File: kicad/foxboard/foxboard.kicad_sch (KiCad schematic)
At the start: 188 parts, among them J1 USB_mini_micro_B, K1 KEYSW, K10 KEYSW, K11 KEYSW, K12 KEYSW, K13 KEYSW, K14 KEYSW, K15 KEYSW, K16 KEYSW, K17 KEYSW, K18 KEYSW, K19 KEYSW, K2 KEYSW, K20 KEYSW, K21 KEYSW, K22 KEYSW, K23 KEYSW, K24 KEYSW, K25 KEYSW, K26 KEYSW, K27 KEYSW, K28 KEYSW, K29 KEYSW, K3 KEYSW, K30 KEYSW, K31 KEYSW, K32 KEYSW, K33 KEYSW, K34 KEYSW, K35 KEYSW, K36 KEYSW, K37 KEYSW, K38 KEYSW, K39 KEYSW, K4 KEYSW, K40 KEYSW, K41 KEYSW, K42 KEYSW, K43 KEYSW, K44 KEYSW, K45 KEYSW, K46 KEYSW, K47 KEYSW, K48 KEYSW, K49 KEYSW, K5 KEYSW, K50 KEYSW, K51 KEYSW, K52 KEYSW, K53 KEYSW, K54 KEYSW, K55 KEYSW, K56 KEYSW, K57 KEYSW, K58 KEYSW, K59 KEYSW, K6 KEYSW, K60 KEYSW, K61 KEYSW, K62 KEYSW, K63 KEYSW, K64 KEYSW, K65 KEYSW, K66 KEYSW, K67 KEYSW, K68 KEYSW, K69 KEYSW, K7 KEYSW, K70 KEYSW, K71 KEYSW, K72 KEYSW, K73 KEYSW, K74 KEYSW, K75 KEYSW, K76 KEYSW, K77 KEYSW, K78 KEYSW, K79 KEYSW, K8 KEYSW, K80 KEYSW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

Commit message: update
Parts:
- removed 10k: R1, symbol Device:R
- removed C1, C2: 22p, symbol Device:C_Small
- removed C8: 1U, symbol Device:C
- removed J1: USB_mini_micro_B, symbol keyboard_parts:USB_mini_micro_B
- removed R2: 10k, symbol Device:R
- removed R3, R4: 22, symbol Device:R
- removed SW1: SW_PUSH, symbol keyboard_parts:SW_PUSH
- removed U1: ATMEGA32U4, symbol keyboard_parts:ATMEGA32U4
- removed X1: XTAL_GND, symbol keyboard_parts:XTAL_GND
- added J2: USB_C_Receptacle_USB2.0, Connector_USB:USB_C_Receptacle_Amphenol_12401548E4-2A, symbol Connector:USB_C_Receptacle_USB2.0
- added R5, R6: 5k1, Resistor_SMD:R_0805_2012Metric_Pad1.20x1.40mm_HandSolder, symbol Device:R
- added U2: Teensy4.1, teensy:Teensy41, symbol teensy:Teensy4.1
- C3, C4, C5, C6: footprint (none) -> Capacitor_SMD:C_0201_0603Metric_Pad0.64x0.40mm_HandSolder
- C7: value 4.7i -> 4.7u; footprint (none) -> Capacitor_SMD:C_0201_0603Metric_Pad0.64x0.40mm_HandSolder
- D1, D10, D11, D12, D13, D14, D15, D16, D17, D18, D19, D2, D20, D21, D22, D23, D24, D25, D26, D27, D28, D29, D3, D30, D31, D32, D33, D34, D35, D36, D37, D38, D39, D4, D40, D41, D42, D43, D44, D45, D46, D47, D48, D49, D5, D50, D51, D52, D53, D54, D55, D56, D57, D58, D59, D6, D60, D61, D62, D63, D64, D65, D66, D67, D68, D69, D7, D70, D71, D72, D73, D74, D75, D76, D77, D78, D79, D8, D80, D81, D82, D83, D84, D85, D86, D9: footprint (none) -> Diode_SMD:D_0201_0603Metric_Pad0.64x0.40mm_HandSolder
- K1, K2, K3, K5, K6, K7, K8: footprint (none) -> PCM_marbastlib-mx:SW_MX_1.25u
- K10, K11, K13, K14, K15, K16, K17, K18, K19, K20, K21, K22, K24, K26, K27, K28, K29, K30, K31, K32, K33, K34, K35, K36, K39, K40, K41, K42, K43, K44, K45, K46, K47, K48, K49, K50, K52, K53, K54, K55, K56, K57, K58, K59, K60, K61, K62, K63, K64, K65, K66, K67, K68, K70, K71, K72, K73, K74, K75, K76, K77, K78, K79, K80, K81, K82, K83, K84, K85, K86, K9: footprint (none) -> PCM_marbastlib-mx:SW_MX_1u
- K12, K23: footprint (none) -> PCM_marbastlib-xp-plate-mx:Plate_MX_SPLIT-RSHIFT
- K25: footprint (none) -> PCM_marbastlib-mx:STAB_MX_2.25u
- K37: footprint (none) -> PCM_marbastlib-mx:STAB_MX_ISO
- K38, K51: footprint (none) -> PCM_marbastlib-mx:SW_MX_1.75u
- K4: footprint (none) -> Mounting_Keyboard_Stabilizer:Stabilizer_Cherry_MX_6.25u
- K69: footprint (none) -> PCM_marbastlib-mx:STAB_MX_2.75u
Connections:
- net +5V: now also R5.1, R6.1
- net at K20.1, K33.1, K45.1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: now also K5.1; no longer K8.1
- net at K21.1, K34.1, K46.1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: now also K6.1
- net at K18.1, K31.1, K43.1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: no longer K6.1
- net at K19.1, K32.1, K44.1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: no longer K7.1
- net at K23.1, K36.1, K49.1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: now also K8.1
- net at K22.1: now also K35.1, K48.1, K65.1, K7.1, K80.1
- net at K16.1, K29.1, K41.1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: no longer K5.1
- net at K15.1, K28.1, K40.1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: no longer K4.1
- net at K17.1, K30.1, K42.1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: now also K4.1
- new net: J2.A1 (GND), J2.A12 (GND), J2.B1 (GND), J2.B12 (GND), J2.S1 (SHIELD), U2.47 (GND)
- new net: J2.A4 (VBUS), J2.A9 (VBUS), J2.B4 (VBUS), J2.B9 (VBUS), U2.48 (VIN)
- new net: J2.A7 (D-), J2.B7 (D-), U2.66 (D-)
- new net: J2.A6 (D+), J2.B6 (D+), U2.67 (D+)
- new net: J2.A5 (CC1), R5.2
- new net: J2.B5 (CC2), R6.2
- no-connect marks 0 -> 2
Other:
- moved on the sheet: D4, D5, D6, D7, D8, K4, K5, K6, K7, K8

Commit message: update
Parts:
- added D87: D, symbol Device:D
- added K87: KEYSW, PCM_marbastlib-mx:SW_MX_1u, symbol keyboard_parts:KEYSW
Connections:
- net at D54.1 (K), D55.1 (K), D56.1 (K)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: now also D87.1 (K)
- net at K51.1, K84.1, K9.1: now also K87.1; no longer K68.1
- net at K83.1: now also K68.1
- new net: D87.2 (A), K87.2
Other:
- moved on the sheet: D68, K68
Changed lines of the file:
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@@
   (junction (at 41.91 144.78) (diameter 0) (color 0 0 0 0)
   )
+  (junction (at 298.45 55.88) (diameter 0) (color 0 0 0 0)
+  )
   (junction (at 60.96 71.12) (diameter 0) (color 0 0 0 0)
   )
@@
   (junction (at 214.63 63.5) (diameter 0) (color 0 0 0 0)
   )
+  (junction (at 341.63 24.13) (diameter 0) (color 0 0 0 0)
+  )
   (junction (at 241.3 166.37) (diameter 0) (color 0 0 0 0)
   )
+  (junction (at 342.9 60.96) (diameter 0) (color 0 0 0 0)
+  )
   (junction (at 276.86 55.88) (diameter 0) (color 0 0 0 0)
   )
@@
   (junction (at 135.89 71.12) (diameter 0) (color 0 0 0 0)
   )
+  (junction (at 326.39 55.88) (diameter 0) (color 0 0 0 0)
+  )
   (junction (at 119.38 107.95) (diameter 0) (color 0 0 0 0)
   )
@@
   (junction (at 123.19 36.83) (diameter 0) (color 0 0 0 0)
   )
+  (junction (at 313.69 25.4) (diameter 0) (color 0 0 0 0)
+  )
   (junction (at 363.22 25.4) (diameter 0) (color 0 0 0 0)
   )
@@
   (junction (at 76.2 97.79) (diameter 0) (color 0 0 0 0)
   )
+  (junction (at 341.63 43.18) (diameter 0) (color 0 0 0 0)
+  )
   (junction (at 196.85 63.5) (diameter 0) (color 0 0 0 0)
   )
@@
   (junction (at 347.98 55.88) (diameter 0) (color 0 0 0 0)
   )
-  (junction (at 341.63 24.13) (diameter 0) (color 0 0 0 0)
-  )
   (junction (at 181.61 71.12) (diameter 0) (color 0 0 0 0)
   )
@@
   (junction (at 257.81 55.88) (diameter 0) (color 0 0 0 0)
   )
-  (junction (at 327.66 55.88) (diameter 0) (color 0 0 0 0)
-  )
   (junction (at 113.03 63.5) (diameter 0) (color 0 0 0 0)
   )
@@
   (junction (at 199.39 71.12) (diameter 0) (color 0 0 0 0)
   )
-  (junction (at 342.9 60.96) (diameter 0) (color 0 0 0 0)
-  )
   (junction (at 259.08 78.74) (diameter 0) (color 0 0 0 0)
   )
@@
   (junction (at 62.23 25.4) (diameter 0) (color 0 0 0 0)
   )
-  (junction (at 342.9 44.45) (diameter 0) (color 0 0 0 0)
-  )
   (no_connect (at 242.57 153.67))
   (no_connect (at 242.57 151.13))
@@
     (stroke (width 0) (type default))
   )
+  (wire (pts (xy 326.39 50.8) (xy 326.39 55.88))
+    (stroke (width 0) (type default))
+  )
   (wire (pts (xy 218.44 45.72) (xy 218.44 33.02))
     (stroke (width 0) (type default))
@@
     (stroke (width 0) (type default))
   )
-  (wire (pts (xy 327.66 55.88) (xy 347.98 55.88))
-    (stroke (width 0) (type default))
-  )
   (wire (pts (xy 80.01 106.68) (xy 80.01 107.95))
     (stroke (width 0) (type default))
@@
     (stroke (width 0) (type default))
   )
-  (wire (pts (xy 342.9 44.45) (xy 342.9 60.96))
-    (stroke (width 0) (type default))
-  )
   (wire (pts (xy 222.25 55.88) (xy 240.03 55.88))
     (stroke (width 0) (type default))
@@
     (stroke (width 0) (type default))
   )
-  (wire (pts (xy 327.66 44.45) (xy 327.66 45.72))
+  (wire (pts (xy 297.18 44.45) (xy 298.45 44.45))
     (stroke (width 0) (type default))
   )
@@
     (stroke (width 0) (type default))
   )
+  (wire (pts (xy 341.63 24.13) (xy 341.63 43.18))
+    (stroke (width 0) (type default))
+  )
   (wire (pts (xy 80.01 46.99) (xy 80.01 48.26))
     (stroke (width 0) (type default))
@@
     (stroke (width 0) (type default))
   )
+  (wire (pts (xy 326.39 55.88) (xy 347.98 55.88))
+    (stroke (width 0) (type default))
+  )
   (wire (pts (xy 170.18 36.83) (xy 195.58 36.83))
     (stroke (width 0) (type default))
   )
+  (wire (pts (xy 312.42 43.18) (xy 312.42 44.45))
+    (stroke (width 0) (type default))
+  )
   (wire (pts (xy 157.48 96.52) (xy 157.48 99.06))
     (stroke (width 0) (type default))
@@
     (stroke (width 0) (type default))
   )
+  (wire (pts (xy 341.63 43.18) (xy 342.9 43.18))
+    (stroke (width 0) (type default))
+  )
   (wire (pts (xy 138.43 15.24) (xy 138.43 26.67))
     (stroke (width 0) (type default))
@@
     (stroke (width 0) (type default))
   )
-  (wire (pts (xy 341.63 24.13) (xy 341.63 40.64))
-    (stroke (width 0) (type default))
-  )
   (wire (pts (xy 240.03 176.53) (xy 242.57 176.53))
     (stroke (width 0) (type default))
@@
     (stroke (width 0) (type default))
   )
+  (wire (pts (xy 312.42 43.18) (xy 313.69 43.18))
+    (stroke (width 0) (type default))
+  )
   (wire (pts (xy 347.98 107.95) (xy 347.98 104.14))
     (stroke (width 0) (type default))
@@
     (stroke (width 0) (type default))
   )
-  (wire (pts (xy 341.63 40.64) (xy 342.9 40.64))
-    (stroke (width 0) (type default))
-  )
   (wire (pts (xy 257.81 54.61) (xy 257.81 55.88))
     (stroke (width 0) (type default))
@@
     (stroke (width 0) (type default))
   )
-  (wire (pts (xy 276.86 55.88) (xy 327.66 55.88))
+  (wire (pts (xy 276.86 55.88) (xy 298.45 55.88))
     (stroke (width 0) (type default))
   )
@@
     (stroke (width 0) (type default))
   )
+  (wire (pts (xy 298.45 55.88) (xy 326.39 55.88))
+    (stroke (width 0) (type default))
+  )
   (wire (pts (xy 120.65 88.9) (xy 138.43 88.9))
     (stroke (width 0) (type default))
@@
     (stroke (width 0) (type default))
   )
+  (wire (pts (xy 342.9 43.18) (xy 342.9 60.96))
+    (stroke (width 0) (type default))
+  )
   (wire (pts (xy 57.15 97.79) (xy 55.88 97.79))
     (stroke (width 0) (type default))
@@
     (stroke (width 0) (type default))
   )
-  (wire (pts (xy 327.66 53.34) (xy 327.66 55.88))
+  (wire (pts (xy 298.45 52.07) (xy 298.45 55.88))
     (stroke (width 0) (type default))
   )
@@
     (stroke (width 0) (type default))
   )
-  (wire (pts (xy 203.2 81.28) (xy 204.47 81.28))
+  (wire (pts (xy 313.69 43.18) (xy 313.69 25.4))
     (stroke (width 0) (type default))
   )
-  (wire (pts (xy 342.9 40.64) (xy 342.9 44.45))
+  (wire (pts (xy 203.2 81.28) (xy 204.47 81.28))
     (stroke (width 0) (type default))
   )
@@
     )
   )
+  (symbol (lib_id "keyboard_parts:KEYSW") (at 334.01 43.18 0) (unit 1)
+    (in_bom yes) (on_board yes) (dnp no) (fields_autoplaced)
+    (property "Reference" "K87" (at 334.01 36.83 0)
+      (effects (font (size 1.524 1.524)))
+    )
+    (property "Value" "KEYSW" (at 334.01 45.72 0)
+      (effects (font (size 1.524 1.524)) hide)
+    )
+    (property "Footprint" "PCM_marbastlib-mx:SW_MX_1u" (at 334.01 43.18 0)
+      (effects (font (size 1.524 1.524)) hide)
+    )
+    (property "Datasheet" "" (at 334.01 43.18 0)
+      (effects (font (size 1.524 1.524)))
+    )
+    (pin "1")
+    (pin "2")
+    (instances
+      (project "foxboard"
+        (path "/06390bb7-84c9-4afb-a691-da3db02fcaf4"
+          (reference "K87") (unit 1)
+        )
+      )
+    )
+  )
   (symbol (lib_id "Device:D") (at 259.08 31.75 90) (unit 1)
     (in_bom yes) (on_board yes) (dnp no) (fields_autoplaced)
@@
     )
   )
+  (symbol (lib_id "Device:D") (at 326.39 46.99 90) (unit 1)
+    (in_bom yes) (on_board yes) (dnp no) (fields_autoplaced)
+    (property "Reference" "D87" (at 328.93 45.72 90)
+      (effects (font (size 1.27 1.27)) (justify right))
+    )
+    (property "Value" "D" (at 328.93 48.26 90)
+      (effects (font (size 1.27 1.27)) (justify right))
+    )
+    (property "Footprint" "" (at 326.39 46.99 0)
+      (effects (font (size 1.27 1.27)) hide)
+    )
+    (property "Datasheet" "~" (at 326.39 46.99 0)
+      (effects (font (size 1.27 1.27)) hide)
+    )
+    (property "Sim.Device" "D" (at 326.39 46.99 0)
+      (effects (font (size 1.27 1.27)) hide)
+    )
+    (property "Sim.Pins" "1=K 2=A" (at 326.39 46.99 0)
+      (effects (font (size 1.27 1.27)) hide)
+    )
+    (pin "1")
+    (pin "2")
+    (instances
+      (project "foxboard"
+        (path "/06390bb7-84c9-4afb-a691-da3db02fcaf4"
+          (reference "D87") (unit 1)
+        )
+      )
+    )
+  )
   (symbol (lib_id "Device:D") (at 240.03 50.8 90) (unit 1)
     (in_bom yes) (on_board yes) (dnp no) (fields_autoplaced)
@@
     )
   )
-  (symbol (lib_id "Device:D") (at 327.66 49.53 90) (unit 1)
+  (symbol (lib_id "Device:D") (at 298.45 48.26 90) (unit 1)
     (in_bom yes) (on_board yes) (dnp no) (fields_autoplaced)
-    (property "Reference" "D68" (at 330.2 48.26 90)
+    (property "Reference" "D68" (at 300.99 46.99 90)
       (effects (font (size 1.27 1.27)) (justify right))
     )
-    (property "Value" "D" (at 330.2 50.8 90)
+    (property "Value" "D" (at 300.99 49.53 90)
       (effects (font (size 1.27 1.27)) (justify right))
     )
-    (property "Footprint" "Diode_SMD:D_0201_0603Metric_Pad0.64x0.40mm_HandSolder" (at 327.66 49.53 0)
+    (property "Footprint" "Diode_SMD:D_0201_0603Metric_Pad0.64x0.40mm_HandSolder" (at 298.45 48.26 0)
       (effects (font (size 1.27 1.27)) hide)
     )
-    (property "Datasheet" "~" (at 327.66 49.53 0)
+    (property "Datasheet" "~" (at 298.45 48.26 0)
       (effects (font (size 1.27 1.27)) hide)
     )
-    (property "Sim.Device" "D" (at 327.66 49.53 0)
+    (property "Sim.Device" "D" (at 298.45 48.26 0)
       (effects (font (size 1.27 1.27)) hide)
     )
-    (property "Sim.Pins" "1=K 2=A" (at 327.66 49.53 0)
+    (property "Sim.Pins" "1=K 2=A" (at 298.45 48.26 0)
       (effects (font (size 1.27 1.27)) hide)
     )
@@
     )
   )
-  (symbol (lib_id "keyboard_parts:KEYSW") (at 335.28 44.45 0) (unit 1)
+  (symbol (lib_id "keyboard_parts:KEYSW") (at 304.8 44.45 0) (unit 1)
     (in_bom yes) (on_board yes) (dnp no) (fields_autoplaced)
-    (property "Reference" "K68" (at 335.28 38.1 0)
+    (property "Reference" "K68" (at 304.8 38.1 0)
       (effects (font (size 1.524 1.524)))
     )
-    (property "Value" "KEYSW" (at 335.28 46.99 0)
+    (property "Value" "KEYSW" (at 304.8 46.99 0)
       (effects (font (size 1.524 1.524)) hide)
     )
-    (property "Footprint" "PCM_marbastlib-mx:SW_MX_1u" (at 335.28 44.45 0)
+    (property "Footprint" "PCM_marbastlib-mx:SW_MX_1u" (at 304.8 44.45 0)
       (effects (font (size 1.524 1.524)) hide)
     )
-    (property "Datasheet" "" (at 335.28 44.45 0)
+    (property "Datasheet" "" (at 304.8 44.45 0)
       (effects (font (size 1.524 1.524)))
     )

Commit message: update layout
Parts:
- D87: footprint (none) -> Diode_SMD:D_0201_0603Metric_Pad0.64x0.40mm_HandSolder
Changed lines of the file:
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@@
       (effects (font (size 1.27 1.27)) (justify right))
     )
-    (property "Footprint" "" (at 326.39 46.99 0)
+    (property "Footprint" "Diode_SMD:D_0201_0603Metric_Pad0.64x0.40mm_HandSolder" (at 326.39 46.99 0)
       (effects (font (size 1.27 1.27)) hide)
     )

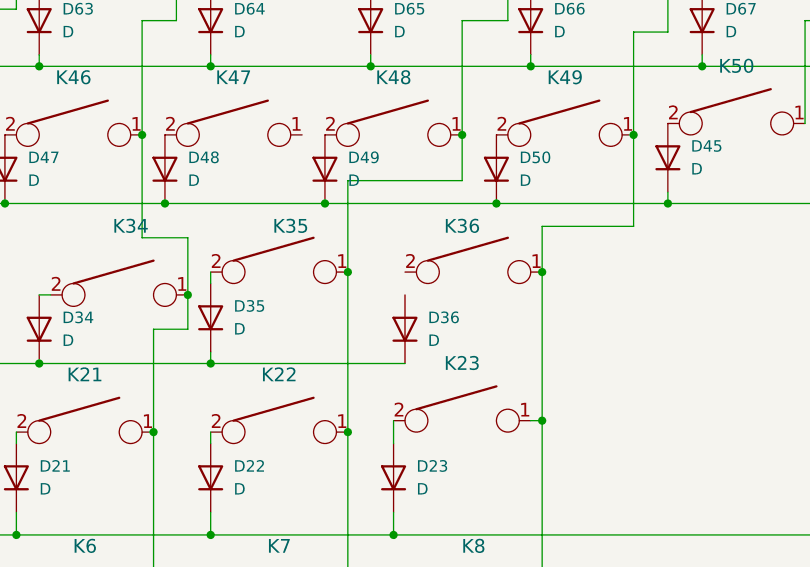
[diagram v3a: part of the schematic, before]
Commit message: update some footprints and move most diodes into place
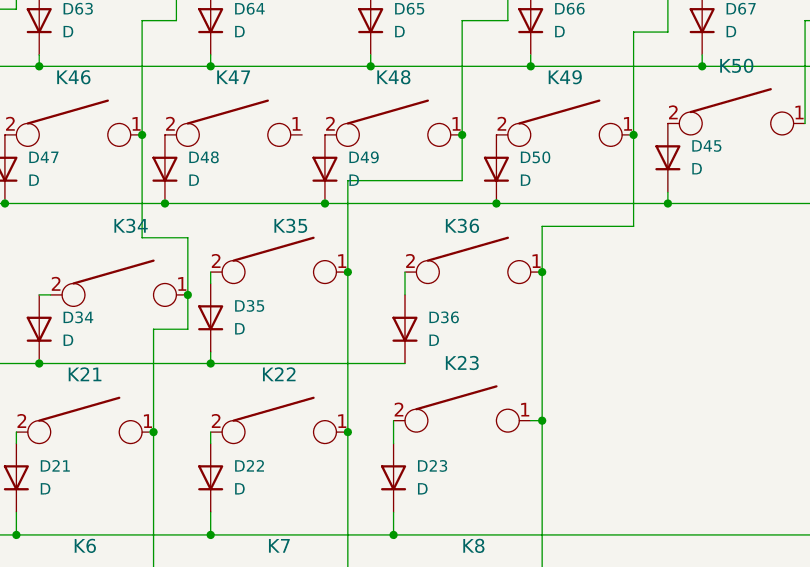
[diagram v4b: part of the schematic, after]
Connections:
- net at K36.2: now also D36.2 (A)
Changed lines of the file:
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@@
+    (stroke (width 0) (type default))
+  )
+  (wire (pts (xy 243.84 78.74) (xy 243.84 81.28))
     (stroke (width 0) (type default))
   )

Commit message: move all resitors, caps and diodes to the back of the pcb
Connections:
- net at D54.1 (K), D55.1 (K), D56.1 (K)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: now also U2.29 (37_CS)
- net at D25.1 (K), D26.1 (K), D27.1 (K)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: now also U2.27 (35_TX8)
- net at K14.1, K27.1, K3.1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: now also U2.33 (41_A17)
- net at K1.1, K12.1, K25.1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: now also U2.31 (39_MISO1_OUT1A)
- net at D71.1 (K), D72.1 (K), D73.1 (K)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: now also U2.30 (38_CS1_IN1)
- net at K10.1, K24.1, K52.1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: now also U2.3 (1_TX1_CTX2_MISO1)
- net at K20.1, K33.1, K45.1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: now also U2.10 (8_TX2_IN1)
- net at K21.1, K34.1, K46.1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: now also U2.9 (7_RX2_OUT1A)
- net at K51.1, K84.1, K87.1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: now also U2.4 (2_OUT2)
- net at K81.1: now also U2.7 (5_IN2)
- net at U2.2 (0_RX1_CRX2_CS1): now also K11.1, K53.1, K70.1, K86.1
- net at U2.25 (33_MCLK2): now also D1.1 (K), D10.1 (K), D11.1 (K), D2.1 (K), D3.1 (K), D4.1 (K), D5.1 (K), D6.1 (K), D7.1 (K), D8.1 (K), D9.1 (K)
- net at U2.26 (34_RX8): now also D12.1 (K), D13.1 (K), D14.1 (K), D15.1 (K), D16.1 (K), D17.1 (K), D18.1 (K), D19.1 (K), D20.1 (K), D21.1 (K), D22.1 (K), D23.1 (K), D24.1 (K)
- net at U2.28 (36_CS): now also D37.1 (K), D38.1 (K), D39.1 (K), D40.1 (K), D41.1 (K), D42.1 (K), D43.1 (K), D44.1 (K), D45.1 (K), D46.1 (K), D47.1 (K), D48.1 (K), D49.1 (K), D50.1 (K), D51.1 (K), D52.1 (K), D53.1 (K)
- net at U2.32 (40_A16): now also K13.1, K2.1, K26.1, K38.1, K55.1, K72.1
- net at U2.35 (13_SCK_LED): now also K15.1, K28.1, K40.1, K57.1
- net at U2.36 (14_A0_TX3_SPDIF_OUT): now also K16.1, K29.1, K41.1, K58.1, K74.1
- net at U2.37 (15_A1_RX3_SPDIF_IN): now also K17.1, K30.1, K4.1, K42.1, K59.1, K75.1
- net at U2.38 (16_A2_RX4_SCL1): now also K18.1, K31.1, K43.1, K60.1, K76.1
- net at U2.39 (17_A3_TX4_SDA1): now also K19.1, K32.1, K44.1, K61.1, K77.1
- net at U2.5 (3_LRCLK2): now also K68.1, K83.1
- net at U2.6 (4_BCLK2): now also K82.1
- net at U2.8 (6_OUT1D): now also K22.1, K35.1, K48.1, K65.1, K7.1, K80.1

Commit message: update footprints
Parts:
- K4: footprint Mounting_Keyboard_Stabilizer:Stabilizer_Cherry_MX_6.25u -> rhais_cherry:MX_KEY_4.45
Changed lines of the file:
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@@
       (effects (font (size 1.524 1.524)) hide)
     )
-    (property "Footprint" "Mounting_Keyboard_Stabilizer:Stabilizer_Cherry_MX_6.25u" (at 120.65 115.57 0)
+    (property "Footprint" "rhais_cherry:MX_KEY_4.45" (at 120.65 115.57 0)
       (effects (font (size 1.524 1.524)) hide)
     )

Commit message: add rows
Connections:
- net at D55.1 (K), D56.1 (K), D57.1 (K)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: now also U2.26 (34_RX8); no longer D54.1 (K), U2.29 (37_CS)
- net at D25.1 (K), D26.1 (K), D27.1 (K)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: now also D37.1 (K), U2.17 (25_A11_RX6_SDA2); no longer U2.27 (35_TX8)
- net at K14.1, K27.1, K3.1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: no longer U2.33 (41_A17)
- net at K1.1, K12.1, K25.1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: no longer K37.1, K54.1, U2.31 (39_MISO1_OUT1A)
- net at D71.1 (K), D72.1 (K), D73.1 (K)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: now also U2.25 (33_MCLK2); no longer U2.30 (38_CS1_IN1)
- net at K10.1, K24.1, K69.1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: now also K53.1; no longer K52.1, U2.3 (1_TX1_CTX2_MISO1)
- net at K20.1, K33.1, K45.1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: no longer U2.10 (8_TX2_IN1)
- net at K45.2: now also D45.2 (A); no longer D46.2 (A)
- net at K21.1, K34.1, K46.1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: no longer U2.9 (7_RX2_OUT1A)
- net at K84.1, K87.1, K9.1: now also K52.1; no longer K51.1, U2.4 (2_OUT2)
- net at K81.1: no longer U2.7 (5_IN2)
- net at K11.1, K70.1, K86.1: now also K54.1; no longer K53.1, U2.2 (0_RX1_CRX2_CS1)
- net at U2.22 (30_CRX3): now also D38.1 (K), D39.1 (K), D40.1 (K), D41.1 (K), D42.1 (K), D43.1 (K), D44.1 (K), D45.1 (K), D46.1 (K), D47.1 (K), D48.1 (K), D49.1 (K), D50.1 (K), D51.1 (K), D52.1 (K), D53.1 (K), D54.1 (K)
- net at U2.23 (31_CTX3): now also D12.1 (K), D13.1 (K), D14.1 (K), D15.1 (K), D16.1 (K), D17.1 (K), D18.1 (K), D19.1 (K), D20.1 (K), D21.1 (K), D22.1 (K), D23.1 (K), D24.1 (K)
- net at U2.24 (32_OUT1B): now also D1.1 (K), D10.1 (K), D11.1 (K), D2.1 (K), D3.1 (K), D4.1 (K), D5.1 (K), D6.1 (K), D7.1 (K), D8.1 (K), D9.1 (K)
- net at K13.1, K2.1, K26.1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: no longer U2.32 (40_A16)
- net at K15.1, K28.1, K40.1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: no longer U2.35 (13_SCK_LED)
- net at K16.1, K29.1, K41.1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: no longer U2.36 (14_A0_TX3_SPDIF_OUT)
- net at K17.1, K30.1, K4.1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: no longer U2.37 (15_A1_RX3_SPDIF_IN)
- net at K18.1, K31.1, K43.1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: no longer U2.38 (16_A2_RX4_SCL1)
- net at K19.1, K32.1, K44.1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: no longer U2.39 (17_A3_TX4_SDA1)
- net at K68.1, K83.1: now also K51.1; no longer U2.5 (3_LRCLK2)
- net at U2.6 (4_BCLK2): no longer K82.1
- net at K22.1, K35.1, K48.1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: no longer U2.8 (6_OUT1D)
- net at D48.2 (A): now also K48.2; no longer K47.2
- net at K49.2: now also D49.2 (A); no longer D50.2 (A)
- net at K50.2: now also D50.2 (A); no longer D45.2 (A)
- net at K70.2: now also D70.2 (A)
- net at K50.1, K67.1: now also K37.1
- net at D47.2 (A): now also K47.2; no longer K46.2
- new net: D46.2 (A), K46.2
- now unconnected: U2.28 (36_CS)
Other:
- moved on the sheet: D45, D46, D47, D48, D49, D50, D51, D52, D53, D70, K51, K52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
